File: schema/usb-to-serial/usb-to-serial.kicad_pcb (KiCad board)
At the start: 2 copper layers, 29 x 57 mm, 36 parts, among them P1 CONN_6X2, Q1 MOS_P, U1 FT232BL, U2 LP5951MF-3.3, U3 MINI-USB-B, X1 CRYSTAL

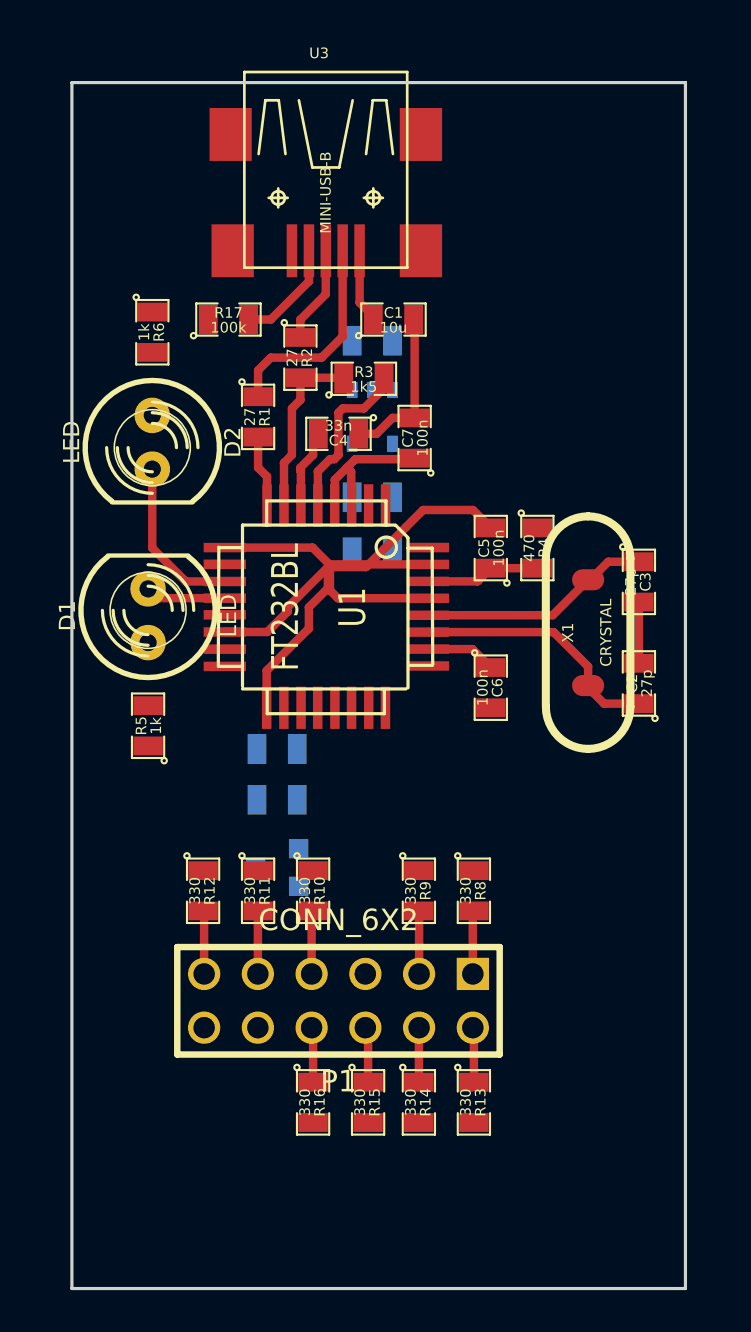
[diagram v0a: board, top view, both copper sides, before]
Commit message: Changed scheme for easier routing.
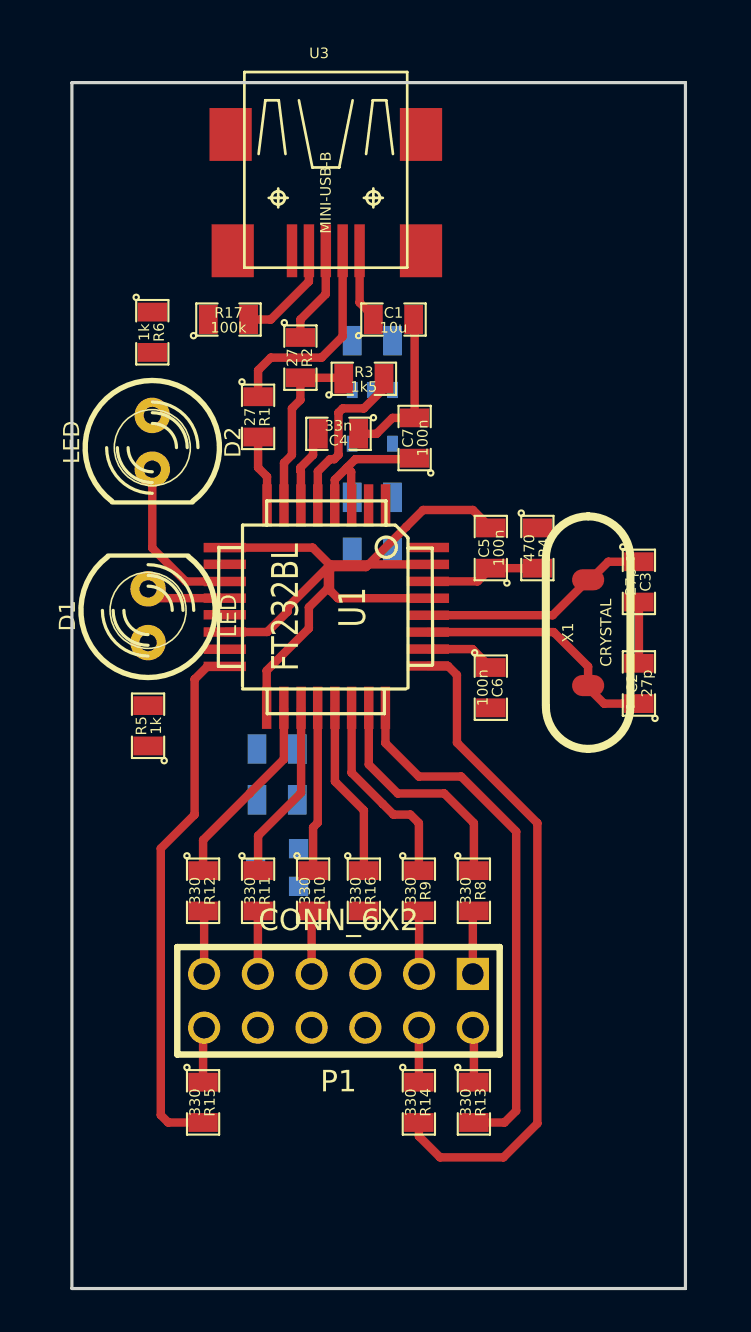
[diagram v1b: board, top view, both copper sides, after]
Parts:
- moved R16 10.3 mm to (195.8, 140.2)
- moved R15 7.80 mm to (188.2, 150.2)
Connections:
- P1 pad 10: /vccout -> +3.3V
- P1 pad 12: +3.3V -> N-000001
- P1 pad 5: GND -> N-0000023
- P1 pad 6: N-000008 -> GND
- P1 pad 8: N-000007 -> /vccout
- R10 pad 1: /rts -> /dsr
- R11 pad 1: /dtr -> /dcd
- R12 pad 1: /txden -> /ri
- R13 pad 2: /cts -> /rxd
- R14 pad 2: /dsr -> /txd
- R15 pad 1: N-000008 -> N-000001
- R15 pad 2: /dcd -> /txden
- R16 pad 1: N-000007 -> /dtr
- R16 pad 2: /ri -> N-0000023
- R8 pad 1: /txd -> /rts
- R9 pad 1: /rxd -> /cts
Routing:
- net /txd: track 0.00 -> 31.6 mm
- net /txden: track 0.00 -> 25.1 mm
- net /rxd: track 0.00 -> 25.0 mm
- net /rts: track 0.00 -> 11.0 mm
- net /cts: track 0.00 -> 9.48 mm
- net /ri: track 0.00 -> 9.28 mm
- net /dcd: track 0.00 -> 8.54 mm
- net /dtr: track 0.00 -> 8.26 mm
- net /dsr: track 0.00 -> 7.79 mm
- net N-000008: track 2.63 -> 0.00 mm
- net N-000007: track 2.61 -> 0.00 mm
- net N-000001: track 0.00 -> 2.60 mm
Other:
- net class Default: trace_width 0.254 -> 0.4

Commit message: Added zone to prevent via or route under the socket.
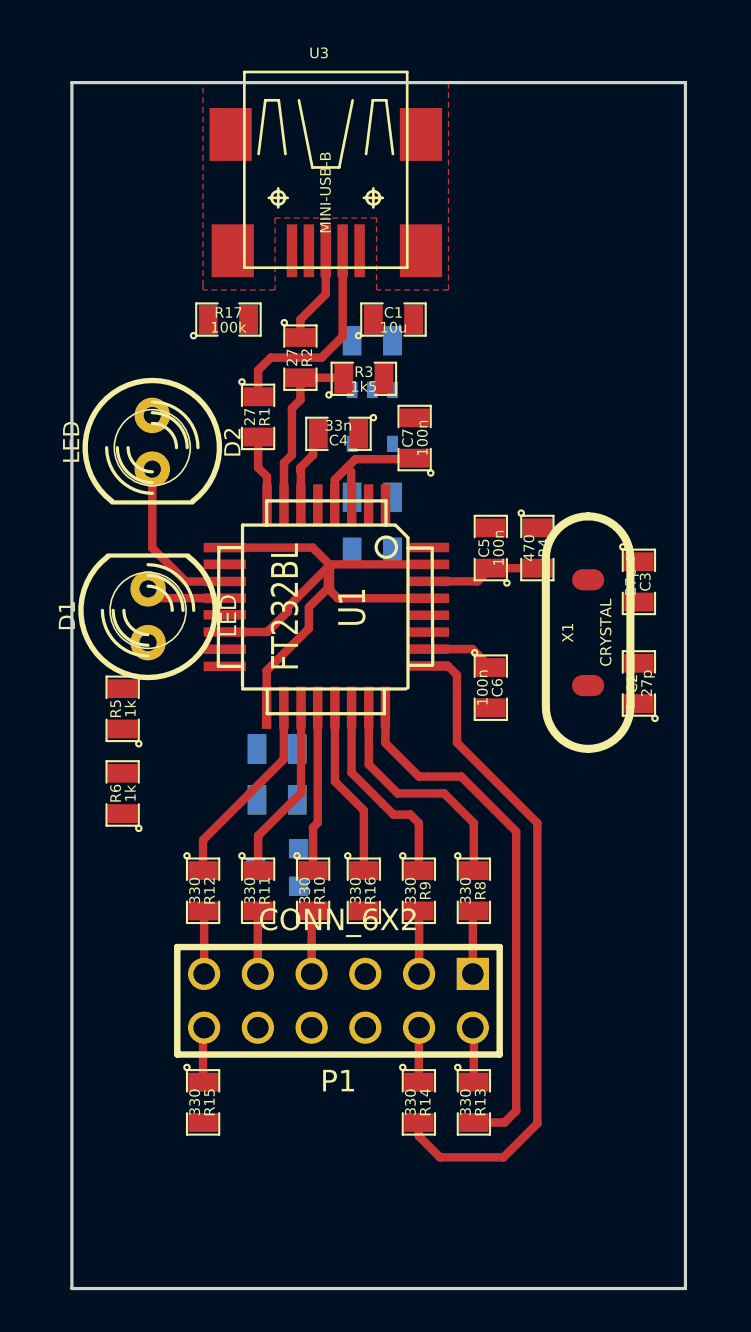
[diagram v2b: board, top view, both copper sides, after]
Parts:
- moved R6 21.8 mm to (184.4, 135.6), turned to 90 degrees
- moved R5 1.44 mm to (184.4, 131.6)
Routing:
- net /txden: track 25.1 -> 0.00 mm
- net GND: track 49.9 -> 30.2 mm
- net /xtal1: track 12.0 -> 0.00 mm
- net /xtal2: track 11.0 -> 0.00 mm
- net /rstout: track 7.98 -> 0.00 mm
- net N-0000025: track 5.05 -> 0.00 mm
- net VCC: track 14.1 -> 10.6 mm
- added copper zone on F.Cu, net GND
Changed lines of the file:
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@@
   (general
     (links 80)
-    (no_connects 35)
+    (no_connects 47)
     (area 181.11055 100.06006 211.075001 159.075001)
     (thickness 1.6)
     (drawings 4)
-    (tracks 160)
+    (tracks 116)
     (zones 0)
     (modules 36)
@@
     (user_trace_width 0.6)
     (trace_clearance 0.254)
-    (zone_clearance 0.508)
+    (zone_clearance 1)
     (zone_45_only no)
     (trace_min 0.254)
@@
   )
   (module SM0805 (layer F.Cu)
-    (at 185.8 113.8 270)
-    (attr smd)
-    (fp_text reference R6 (at 0 -0.3175 270) (layer F.SilkS)
-      (effects (font (size 0.50038 0.50038) (thickness 0.10922)))
-    )
-    (fp_text value 1k (at 0 0.381 270) (layer F.SilkS)
-      (effects (font (size 0.50038 0.50038) (thickness 0.10922)))
-    )
-    (fp_circle (center -1.651 0.762) (end -1.651 0.635) (layer F.SilkS) (width 0.09906))
-    (fp_line (start -0.508 0.762) (end -1.524 0.762) (layer F.SilkS) (width 0.09906))
-    (fp_line (start -1.524 0.762) (end -1.524 -0.762) (layer F.SilkS) (width 0.09906))
-    (fp_line (start -1.524 -0.762) (end -0.508 -0.762) (layer F.SilkS) (width 0.09906))
-    (fp_line (start 0.508 -0.762) (end 1.524 -0.762) (layer F.SilkS) (width 0.09906))
-    (fp_line (start 1.524 -0.762) (end 1.524 0.762) (layer F.SilkS) (width 0.09906))
-    (fp_line (start 1.524 0.762) (end 0.508 0.762) (layer F.SilkS) (width 0.09906))
-    (pad 1 smd rect (at -0.9525 0 270) (size 0.889 1.397)
+    (at 184.4 135.6 90)
+    (attr smd)
+    (fp_text reference R6 (at 0 -0.3175 90) (layer F.SilkS)
+      (effects (font (size 0.50038 0.50038) (thickness 0.10922)))
+    )
+    (fp_text value 1k (at 0 0.381 90) (layer F.SilkS)
+      (effects (font (size 0.50038 0.50038) (thickness 0.10922)))
+    )
+    (fp_circle (center -1.651 0.762) (end -1.651 0.635) (layer F.SilkS) (width 0.09906))
+    (fp_line (start -0.508 0.762) (end -1.524 0.762) (layer F.SilkS) (width 0.09906))
+    (fp_line (start -1.524 0.762) (end -1.524 -0.762) (layer F.SilkS) (width 0.09906))
+    (fp_line (start -1.524 -0.762) (end -0.508 -0.762) (layer F.SilkS) (width 0.09906))
+    (fp_line (start 0.508 -0.762) (end 1.524 -0.762) (layer F.SilkS) (width 0.09906))
+    (fp_line (start 1.524 -0.762) (end 1.524 0.762) (layer F.SilkS) (width 0.09906))
+    (fp_line (start 1.524 0.762) (end 0.508 0.762) (layer F.SilkS) (width 0.09906))
+    (pad 1 smd rect (at -0.9525 0 90) (size 0.889 1.397)
       (layers F.Cu F.Paste F.Mask)
       (net 38 VCC)
     )
-    (pad 2 smd rect (at 0.9525 0 270) (size 0.889 1.397)
+    (pad 2 smd rect (at 0.9525 0 90) (size 0.889 1.397)
       (layers F.Cu F.Paste F.Mask)
       (net 34 N-0000037)
@@
   )
   (module SM0805 (layer F.Cu)
-    (at 185.6 132.4 90)
+    (at 184.4 131.6 90)
     (attr smd)
     (fp_text reference R5 (at 0 -0.3175 90) (layer F.SilkS)
@@
   (segment (start 192.0188 131.5498) (end 192.0188 133.9812) (width 0.4) (layer F.Cu) (net 9))
   (segment (start 192.0188 133.9812) (end 190.4 135.6) (width 0.4) (layer F.Cu) (net 9))
-  (segment (start 193.62408 121.98416) (end 193.62408 120.37592) (width 0.4) (layer F.Cu) (net 10))
-  (segment (start 196.7525 116.4475) (end 196.7525 116) (width 0.4) (layer F.Cu) (net 10))
-  (segment (start 195.8 117.4) (end 196.7525 116.4475) (width 0.4) (layer F.Cu) (net 10))
-  (segment (start 194.8 117.4) (end 195.8 117.4) (width 0.4) (layer F.Cu) (net 10))
-  (segment (start 194.6 117.6) (end 194.8 117.4) (width 0.4) (layer F.Cu) (net 10))
-  (segment (start 194.6 119.6) (end 194.6 117.6) (width 0.4) (layer F.Cu) (net 10))
-  (segment (start 194.4 119.8) (end 194.6 119.6) (width 0.4) (layer F.Cu) (net 10))
-  (segment (start 194.2 119.8) (end 194.4 119.8) (width 0.4) (layer F.Cu) (net 10))
-  (segment (start 193.62408 120.37592) (end 194.2 119.8) (width 0.4) (layer F.Cu) (net 10))
   (segment (start 196.032 131.5498) (end 196.032 134.232) (width 0.4) (layer F.Cu) (net 11))
   (segment (start 201 137) (end 201 139.2475) (width 0.4) (layer F.Cu) (net 11))
@@
   (segment (start 200.2 130) (end 200.2 133.2) (width 0.4) (layer F.Cu) (net 14))
   (segment (start 199.77368 129.57368) (end 200.2 130) (width 0.4) (layer F.Cu) (net 14))
-  (segment (start 189.2248 129.594) (end 188.406 129.594) (width 0.4) (layer F.Cu) (net 15) (status C00000))
-  (segment (start 186.5525 151.1525) (end 188.2 151.1525) (width 0.4) (layer F.Cu) (net 15) (status 800000))
-  (segment (start 186.2 150.8) (end 186.5525 151.1525) (width 0.4) (layer F.Cu) (net 15))
-  (segment (start 186.2 138.2) (end 186.2 150.8) (width 0.4) (layer F.Cu) (net 15))
-  (segment (start 187.8 136.6) (end 186.2 138.2) (width 0.4) (layer F.Cu) (net 15))
-  (segment (start 187.8 130.2) (end 187.8 136.6) (width 0.4) (layer F.Cu) (net 15))
-  (segment (start 188.406 129.594) (end 187.8 130.2) (width 0.4) (layer F.Cu) (net 15) (status 400000))
   (segment (start 189.2248 126.3682) (end 186.0382 126.3682) (width 0.4) (layer F.Cu) (net 16))
   (segment (start 186.0382 126.3682) (end 185.6 125.93) (width 0.4) (layer F.Cu) (net 16))
-  (segment (start 206.4 130.49936) (end 206.4 130.6) (width 0.4) (layer F.Cu) (net 18))
-  (segment (start 207.1525 131.3525) (end 208.8 131.3525) (width 0.4) (layer F.Cu) (net 18))
-  (segment (start 206.4 130.6) (end 207.1525 131.3525) (width 0.4) (layer F.Cu) (net 18))
-  (segment (start 198.826 127.97348) (end 204.77348 127.97348) (width 0.4) (layer F.Cu) (net 18))
-  (segment (start 206.4 129.6) (end 206.4 130.49936) (width 0.4) (layer F.Cu) (net 18))
-  (segment (start 204.77348 127.97348) (end 206.4 129.6) (width 0.4) (layer F.Cu) (net 18))
-  (segment (start 206.4 125.50064) (end 206.49936 125.50064) (width 0.4) (layer F.Cu) (net 19))
-  (segment (start 207.3525 124.6475) (end 208.8 124.6475) (width 0.4) (layer F.Cu) (net 19))
-  (segment (start 206.49936 125.50064) (end 207.3525 124.6475) (width 0.4) (layer F.Cu) (net 19))
-  (segment (start 198.826 127.17592) (end 204.72472 127.17592) (width 0.4) (layer F.Cu) (net 19))
-  (segment (start 204.72472 127.17592) (end 206.4 125.50064) (width 0.4) (layer F.Cu) (net 19))
-  (segment (start 194.1 124.9) (end 195.9 124.9) (width 0.4) (layer F.Cu) (net 20))
-  (segment (start 200.9525 122.2) (end 201.8 123.0475) (width 0.4) (layer F.Cu) (net 20))
-  (segment (start 198.6 122.2) (end 200.9525 122.2) (width 0.4) (layer F.Cu) (net 20))
-  (segment (start 197.8 123) (end 198.6 122.2) (width 0.4) (layer F.Cu) (net 20))
-  (segment (start 195.9 124.9) (end 197.8 123) (width 0.4) (layer F.Cu) (net 20))
   (segment (start 194.1 124.9) (end 194.1 125.9) (width 0.4) (layer F.Cu) (net 20))
   (segment (start 191.206 129.794) (end 191.206 131.5498) (width 0.4) (layer F.Cu) (net 20))
@@
   (segment (start 194.2 124.77308) (end 198.826 124.77308) (width 0.4) (layer F.Cu) (net 20))
   (segment (start 193.3806 123.9806) (end 194.17308 124.77308) (width 0.4) (layer F.Cu) (net 20))
-  (segment (start 208.8 129.4475) (end 208.8 126.5525) (width 0.4) (layer F.Cu) (net 20))
-  (segment (start 198.2 117.8475) (end 198.2 113.2475) (width 0.4) (layer F.Cu) (net 20))
-  (segment (start 198.2 113.2475) (end 198.1525 113.2) (width 0.4) (layer F.Cu) (net 20))
-  (segment (start 195.5525 118.6) (end 196.4 118.6) (width 0.4) (layer F.Cu) (net 20))
-  (segment (start 197.1525 117.8475) (end 198.2 117.8475) (width 0.4) (layer F.Cu) (net 20))
-  (segment (start 196.4 118.6) (end 197.1525 117.8475) (width 0.4) (layer F.Cu) (net 20))
-  (segment (start 188.2 149.2475) (end 188.2 146.72) (width 0.4) (layer F.Cu) (net 21) (status C00000))
-  (segment (start 188.2 146.72) (end 188.25 146.67) (width 0.4) (layer F.Cu) (net 21) (status C00000))
+  (segment (start 188.2 149.2475) (end 188.2 146.72) (width 0.4) (layer F.Cu) (net 21))
+  (segment (start 188.2 146.72) (end 188.25 146.67) (width 0.4) (layer F.Cu) (net 21))
   (segment (start 198.4 149.2475) (end 198.4 146.68) (width 0.4) (layer F.Cu) (net 22))
   (segment (start 198.4 146.68) (end 198.41 146.67) (width 0.4) (layer F.Cu) (net 22))
@@
   (segment (start 200.95 144.13) (end 200.95 141.2025) (width 0.4) (layer F.Cu) (net 28))
   (segment (start 200.95 141.2025) (end 201 141.1525) (width 0.4) (layer F.Cu) (net 28))
-  (segment (start 193.20244 109.94828) (end 193.20244 111.39756) (width 0.4) (layer F.Cu) (net 30))
-  (segment (start 191.4 113.2) (end 190.3525 113.2) (width 0.4) (layer F.Cu) (net 30))
-  (segment (start 193.20244 111.39756) (end 191.4 113.2) (width 0.4) (layer F.Cu) (net 30))
   (segment (start 192.82398 121.98416) (end 192.82398 120.37602) (width 0.4) (layer F.Cu) (net 32))
   (segment (start 193.4 118.8475) (end 193.6475 118.6) (width 0.4) (layer F.Cu) (net 32))
@@
   (segment (start 195 120.2) (end 195.2 120.4) (width 0.4) (layer F.Cu) (net 38))
   (segment (start 194.42418 120.77582) (end 195 120.2) (width 0.4) (layer F.Cu) (net 38))
-  (segment (start 196.2475 113.2) (end 196.2475 113.0475) (width 0.4) (layer F.Cu) (net 38))
-  (segment (start 195.59766 112.39766) (end 195.59766 109.94828) (width 0.4) (layer F.Cu) (net 38))
-  (segment (start 196.2475 113.0475) (end 195.59766 112.39766) (width 0.4) (layer F.Cu) (net 38))
+  (zone (net 20) (net_name GND) (layer F.Cu) (hatch edge 0.508)
+    (connect_pads (clearance 1))
+    (min_thickness 0.5)
+    (fill (arc_segments 16) (thermal_gap 5.08) (thermal_bridge_width 5.08))
+    (polygon
+      (pts
+        (xy 199.8 111.8) (xy 196.4 111.8) (xy 196.4 108.4) (xy 191.6 108.4) (xy 191.6 111.8)
+        (xy 188.2 111.8) (xy 188.2 111.6) (xy 188.2 102) (xy 199.8 102)
+      )
+    )
+  )
 )

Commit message: Placing elements.
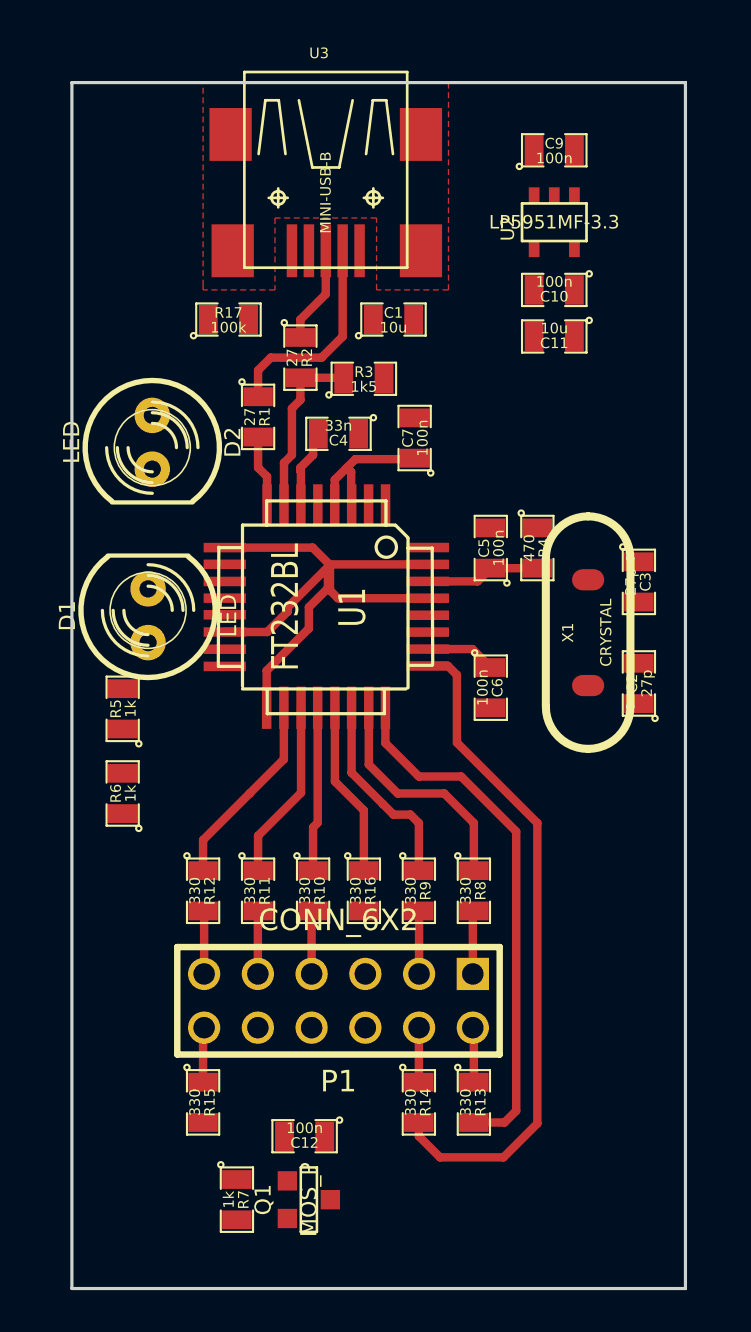
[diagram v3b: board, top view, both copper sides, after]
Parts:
- C10, C11, C12, C9, Q1, R7, U2: moved to F.Cu
- moved R7 21.4 mm to (189.8, 154.8), turned to 270 degrees
- moved C12 16.0 mm to (193.0, 151.8), turned to 180 degrees
- moved Q1 15.8 mm to (193.2, 154.8)
- moved C11 13.3 mm to (204.8, 114.0), turned to 180 degrees
- moved C10 13.0 mm to (204.8, 111.8), turned to 180 degrees
- moved U2 12.6 mm to (204.8, 108.6), turned to 180 degrees
- moved C9 12.4 mm to (204.8, 105.2)
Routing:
- net /rxled: track 7.81 -> 0.00 mm
- net /txled: track 3.81 -> 0.00 mm

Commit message: t
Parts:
- moved D1 12.2 mm to (185.2, 115.0)
- moved R5 11.8 mm to (185.2, 119.8)
- moved R6 11.8 mm to (185.2, 123.8)
- moved D2 11.0 mm to (185.2, 108.0), turned to 90 degrees
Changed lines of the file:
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@@
   (page A3)
   (layers
-    (15 F.Cu signal hide)
+    (15 F.Cu signal)
     (0 B.Cu signal)
     (16 B.Adhes user)
@@
   )
   (module SM0805 (layer F.Cu)
-    (at 184.4 135.6 90)
+    (at 185.2 123.8 90)
     (attr smd)
     (fp_text reference R6 (at 0 -0.3175 90) (layer F.SilkS)
@@
   )
   (module SM0805 (layer F.Cu)
-    (at 184.4 131.6 90)
+    (at 185.2 119.8 90)
     (attr smd)
     (fp_text reference R5 (at 0 -0.3175 90) (layer F.SilkS)
@@
   )
   (module LED-5MM (layer F.Cu)
-    (at 185.8 119 270)
+    (at 185.2 108 90)
     (descr "LED 5mm - Lead pitch 100mil (2,54mm)")
     (tags "LED led 5mm 5MM 100mil 2,54mm")
-    (fp_text reference D2 (at 0 -3.81 270) (layer F.SilkS)
+    (fp_text reference D2 (at 0 -3.81 90) (layer F.SilkS)
       (effects (font (size 0.762 0.762) (thickness 0.0889)))
     )
-    (fp_text value LED (at 0 3.81 270) (layer F.SilkS)
+    (fp_text value LED (at 0 3.81 90) (layer F.SilkS)
       (effects (font (size 0.762 0.762) (thickness 0.0889)))
     )
@@
     (fp_arc (start 0.254 0) (end -1.905 0) (angle 90) (layer F.SilkS) (width 0.1524))
     (fp_arc (start 0.254 0) (end 2.413 0) (angle 90) (layer F.SilkS) (width 0.1524))
-    (pad 1 thru_hole circle (at -1.27 0 270) (size 1.6764 1.6764) (drill 0.812799)
+    (pad 1 thru_hole circle (at -1.27 0 90) (size 1.6764 1.6764) (drill 0.812799)
       (layers *.Cu *.Mask F.SilkS)
       (net 34 N-0000037)
     )
-    (pad 2 thru_hole circle (at 1.27 0 270) (size 1.6764 1.6764) (drill 0.812799)
+    (pad 2 thru_hole circle (at 1.27 0 90) (size 1.6764 1.6764) (drill 0.812799)
       (layers *.Cu *.Mask F.SilkS)
       (net 13 /rxled)
@@
   )
   (module LED-5MM (layer F.Cu)
-    (at 185.6 127.2 90)
+    (at 185.2 115 90)
     (descr "LED 5mm - Lead pitch 100mil (2,54mm)")
     (tags "LED led 5mm 5MM 100mil 2,54mm")
